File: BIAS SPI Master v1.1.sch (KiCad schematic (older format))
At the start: 32 parts, among them J1 Apple ][ Peripheral Connector, J2 SPI Ouput, J3 GND, U1 74LS541, U2 74LS595, U3 74LS165, U4 74LS163, U5 74LS138, U6 74LS00, U7 74LS540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

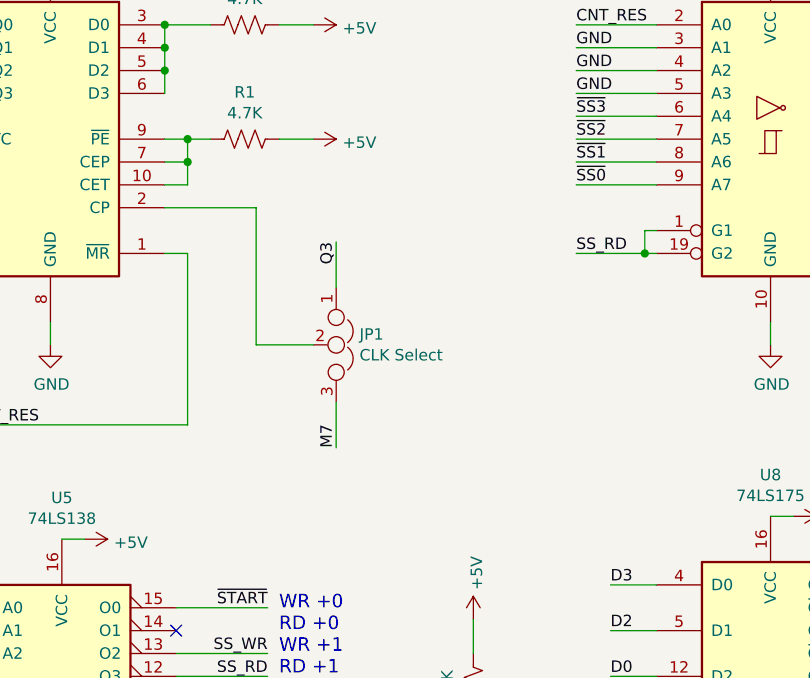
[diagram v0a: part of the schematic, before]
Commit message: Added low pass filter to clean up Apple ][ clock signal ringing
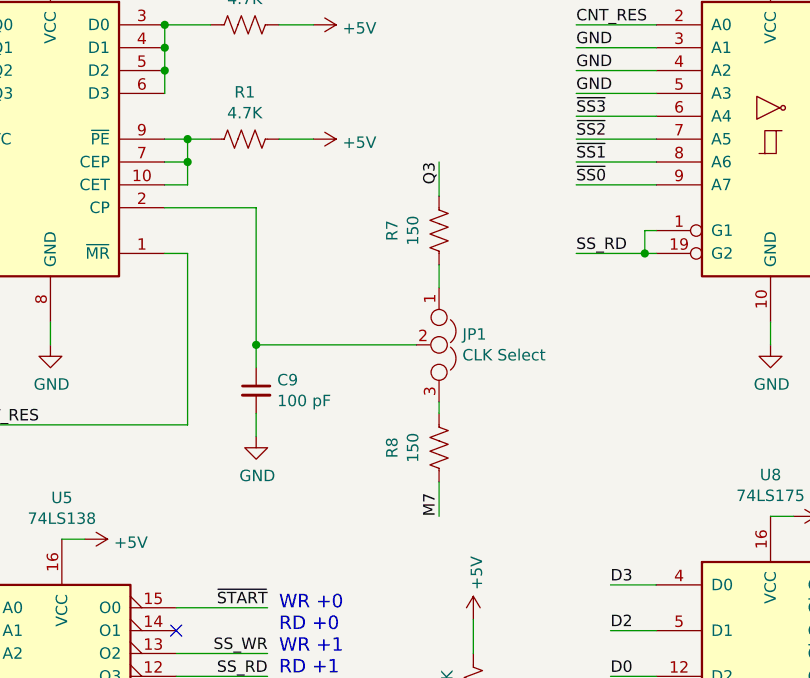
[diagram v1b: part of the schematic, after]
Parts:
- added C9: 100 pF, Capacitor_THT:C_Rect_L7.0mm_W2.0mm_P5.00mm, symbol Device:C_Small
- added R7, R8: 150, Resistor_THT:R_Axial_DIN0207_L6.3mm_D2.5mm_P10.16mm_Horizontal, symbol Device:R_US
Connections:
- net GND: now also C9.2
- net M7: now also R8.2; no longer JP1.3
- net Q3: now also R7.1; no longer JP1.1
- net at JP1.2, U4.2 (CP): now also C9.1
- new net: JP1.1, R7.2
- new net: JP1.3, R8.1
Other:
- moved on the sheet: JP1
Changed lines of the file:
@@
 EESchema Schematic File Version 4
-LIBS:BIAS SPI Master v1.1-cache
 EELAYER 30 0
 EELAYER END
@@
 	0    1    1    0
 $EndComp
-Text Label 8350 2650 3    50   ~ 0
+Text Label 8800 2300 3    50   ~ 0
 Q3
 Wire Wire Line
-	8350 2650 8350 2850
+	8800 2300 8800 2450
 Text Label 4550 3750 0    50   ~ 0
 ~START
@@
 L Device:Jumper_NC_Dual JP1
 U 1 1 5DEF152C
-P 8350 3100
-F 0 "JP1" V 8304 3202 50  0000 L CNN
-F 1 "CLK Select" V 8395 3202 50  0000 L CNN
-F 2 "Connector_PinHeader_2.54mm:PinHeader_1x03_P2.54mm_Vertical" H 8350 3100 50  0001 C CNN
-F 3 "~" H 8350 3100 50  0001 C CNN
-	1    8350 3100
+P 8800 3100
+F 0 "JP1" V 8754 3202 50  0000 L CNN
+F 1 "CLK Select" V 8845 3202 50  0000 L CNN
+F 2 "Connector_PinHeader_2.54mm:PinHeader_1x03_P2.54mm_Vertical" H 8800 3100 50  0001 C CNN
+F 3 "~" H 8800 3100 50  0001 C CNN
+	1    8800 3100
 	0    1    1    0
 $EndComp
 Wire Wire Line
-	8350 3350 8350 3550
-Text Label 8350 3550 1    50   ~ 0
+	8800 3350 8800 3400
+Text Label 8800 3850 1    50   ~ 0
 M7
-Wire Wire Line
-	8250 3100 8000 3100
-Wire Wire Line
-	8000 3100 8000 2500
 Wire Wire Line
 	8000 2500 7600 2500
@@
 Wire Wire Line
 	5100 3300 5100 3550
+$Comp
+L Device:C_Small C9
+U 1 1 5F37D89E
+P 8000 3300
+F 0 "C9" H 8092 3346 50  0000 L CNN
+F 1 "100 pF" H 8092 3255 50  0000 L CNN
+F 2 "Capacitor_THT:C_Rect_L7.0mm_W2.0mm_P5.00mm" H 8000 3300 50  0001 C CNN
+F 3 "~" H 8000 3300 50  0001 C CNN
+	1    8000 3300
+	1    0    0    -1
+$EndComp
+$Comp
+L power:GND #PWR0106
+U 1 1 5F37E4F3
+P 8000 3500
+F 0 "#PWR0106" H 8000 3250 50  0001 C CNN
+F 1 "GND" H 8005 3327 50  0000 C CNN
+F 2 "" H 8000 3500 50  0001 C CNN
+F 3 "" H 8000 3500 50  0001 C CNN
+	1    8000 3500
+	1    0    0    -1
+$EndComp
+Wire Wire Line
+	8000 3400 8000 3500
+$Comp
+L Device:R_US R7
+U 1 1 5F40A979
+P 8800 2600
+F 0 "R7" V 8595 2600 50  0000 C CNN
+F 1 "150" V 8686 2600 50  0000 C CNN
+F 2 "Resistor_THT:R_Axial_DIN0207_L6.3mm_D2.5mm_P10.16mm_Horizontal" V 8840 2590 50  0001 C CNN
+F 3 "~" H 8800 2600 50  0001 C CNN
+	1    8800 2600
+	1    0    0    -1
+$EndComp
+$Comp
+L Device:R_US R8
+U 1 1 5F46BBAB
+P 8800 3550
+F 0 "R8" V 8595 3550 50  0000 C CNN
+F 1 "150" V 8686 3550 50  0000 C CNN
+F 2 "Resistor_THT:R_Axial_DIN0207_L6.3mm_D2.5mm_P10.16mm_Horizontal" V 8840 3540 50  0001 C CNN
+F 3 "~" H 8800 3550 50  0001 C CNN
+	1    8800 3550
+	1    0    0    -1
+$EndComp
+Wire Wire Line
+	8800 3700 8800 3850
+Wire Wire Line
+	8800 2750 8800 2850
+Wire Wire Line
+	8000 2500 8000 3100
+Wire Wire Line
+	8700 3100 8000 3100
+Connection ~ 8000 3100
+Wire Wire Line
+	8000 3100 8000 3200
 $EndSCHEMATC

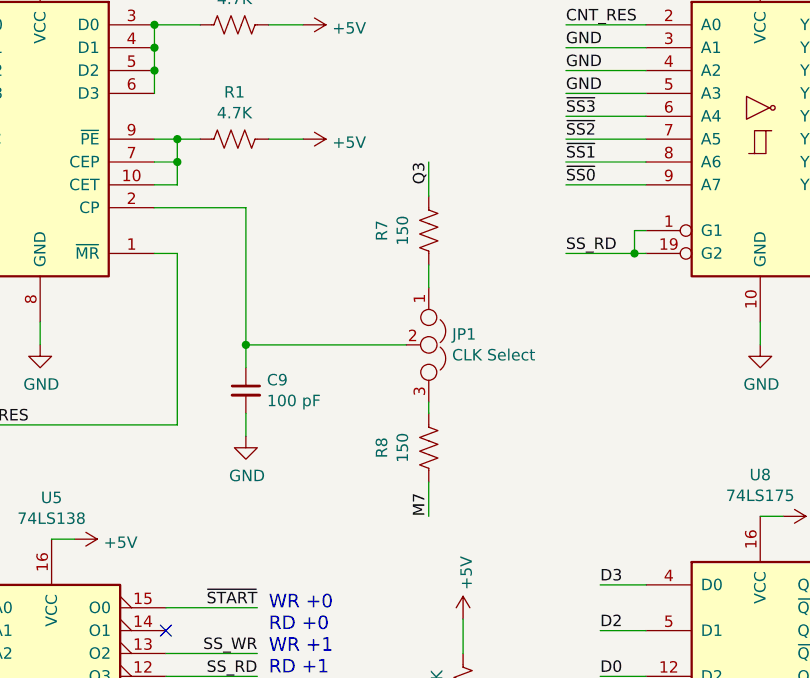
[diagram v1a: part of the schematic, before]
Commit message: Fixed RC filter schematic and PCB
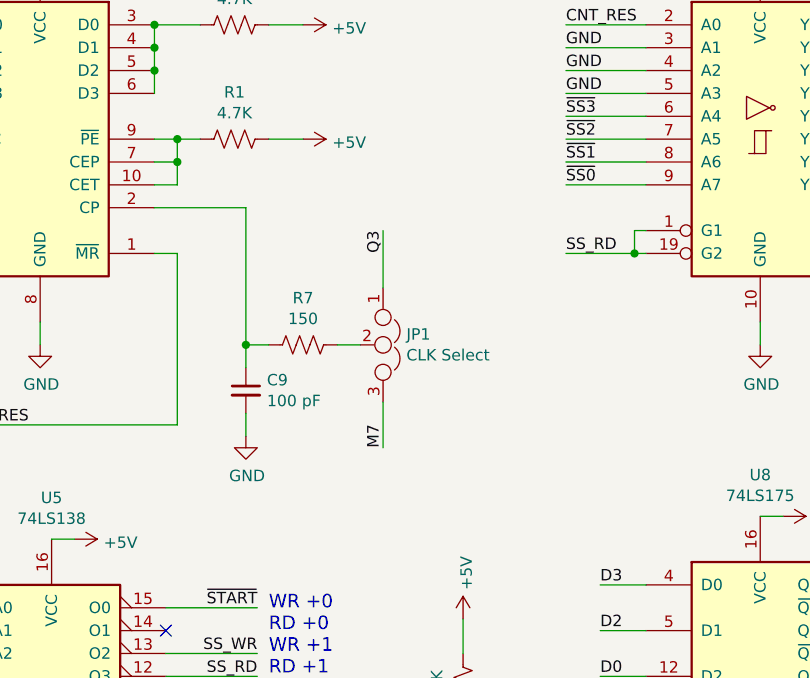
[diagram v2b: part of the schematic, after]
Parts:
- removed R8: 150, Resistor_THT:R_Axial_DIN0207_L6.3mm_D2.5mm_P10.16mm_Horizontal, symbol Device:R_US
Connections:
- net M7: now also JP1.3
- net Q3: now also JP1.1; no longer R7.1
- net at C9.1, U4.2 (CP): now also R7.2; no longer JP1.2
- new net: JP1.2, R7.1
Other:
- moved on the sheet: JP1, R7
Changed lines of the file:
@@
 	0    1    1    0
 $EndComp
-Text Label 8800 2300 3    50   ~ 0
+Text Label 8600 2600 3    50   ~ 0
 Q3
-Wire Wire Line
-	8800 2300 8800 2450
 Text Label 4550 3750 0    50   ~ 0
 ~START
@@
 L Device:Jumper_NC_Dual JP1
 U 1 1 5DEF152C
-P 8800 3100
-F 0 "JP1" V 8754 3202 50  0000 L CNN
-F 1 "CLK Select" V 8845 3202 50  0000 L CNN
-F 2 "Connector_PinHeader_2.54mm:PinHeader_1x03_P2.54mm_Vertical" H 8800 3100 50  0001 C CNN
-F 3 "~" H 8800 3100 50  0001 C CNN
-	1    8800 3100
-	0    1    1    0
-$EndComp
-Wire Wire Line
-	8800 3350 8800 3400
-Text Label 8800 3850 1    50   ~ 0
+P 8600 3100
+F 0 "JP1" V 8554 3202 50  0000 L CNN
+F 1 "CLK Select" V 8645 3202 50  0000 L CNN
+F 2 "Connector_PinHeader_2.54mm:PinHeader_1x03_P2.54mm_Vertical" H 8600 3100 50  0001 C CNN
+F 3 "~" H 8600 3100 50  0001 C CNN
+	1    8600 3100
+	0    1    1    0
+$EndComp
+Text Label 8600 3550 1    50   ~ 0
 M7
 Wire Wire Line
@@
 L Device:R_US R7
 U 1 1 5F40A979
-P 8800 2600
-F 0 "R7" V 8595 2600 50  0000 C CNN
-F 1 "150" V 8686 2600 50  0000 C CNN
-F 2 "Resistor_THT:R_Axial_DIN0207_L6.3mm_D2.5mm_P10.16mm_Horizontal" V 8840 2590 50  0001 C CNN
-F 3 "~" H 8800 2600 50  0001 C CNN
-	1    8800 2600
-	1    0    0    -1
-$EndComp
-$Comp
-L Device:R_US R8
-U 1 1 5F46BBAB
-P 8800 3550
-F 0 "R8" V 8595 3550 50  0000 C CNN
-F 1 "150" V 8686 3550 50  0000 C CNN
-F 2 "Resistor_THT:R_Axial_DIN0207_L6.3mm_D2.5mm_P10.16mm_Horizontal" V 8840 3540 50  0001 C CNN
-F 3 "~" H 8800 3550 50  0001 C CNN
-	1    8800 3550
-	1    0    0    -1
-$EndComp
-Wire Wire Line
-	8800 3700 8800 3850
-Wire Wire Line
-	8800 2750 8800 2850
+P 8250 3100
+F 0 "R7" V 8045 3100 50  0000 C CNN
+F 1 "150" V 8136 3100 50  0000 C CNN
+F 2 "Resistor_THT:R_Axial_DIN0207_L6.3mm_D2.5mm_P10.16mm_Horizontal" V 8290 3090 50  0001 C CNN
+F 3 "~" H 8250 3100 50  0001 C CNN
+	1    8250 3100
+	0    1    1    0
+$EndComp
 Wire Wire Line
 	8000 2500 8000 3100
 Wire Wire Line
-	8700 3100 8000 3100
+	8100 3100 8000 3100
 Connection ~ 8000 3100
 Wire Wire Line
 	8000 3100 8000 3200
+Wire Wire Line
+	8400 3100 8500 3100
+Wire Wire Line
+	8600 2600 8600 2850
+Wire Wire Line
+	8600 3350 8600 3550
 $EndSCHEMATC
